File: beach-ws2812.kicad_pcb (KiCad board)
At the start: 4 copper layers, 260 x 120 mm, 103 parts, among them CON101 BARREL_JACK, P101 CONN_01X03, SW101 Pushbutton, SW102 Pushbutton, U101 STM32F103C(8-B)Tx, U102 LM1117-3.3, U103 MAX811, X101 8MHz

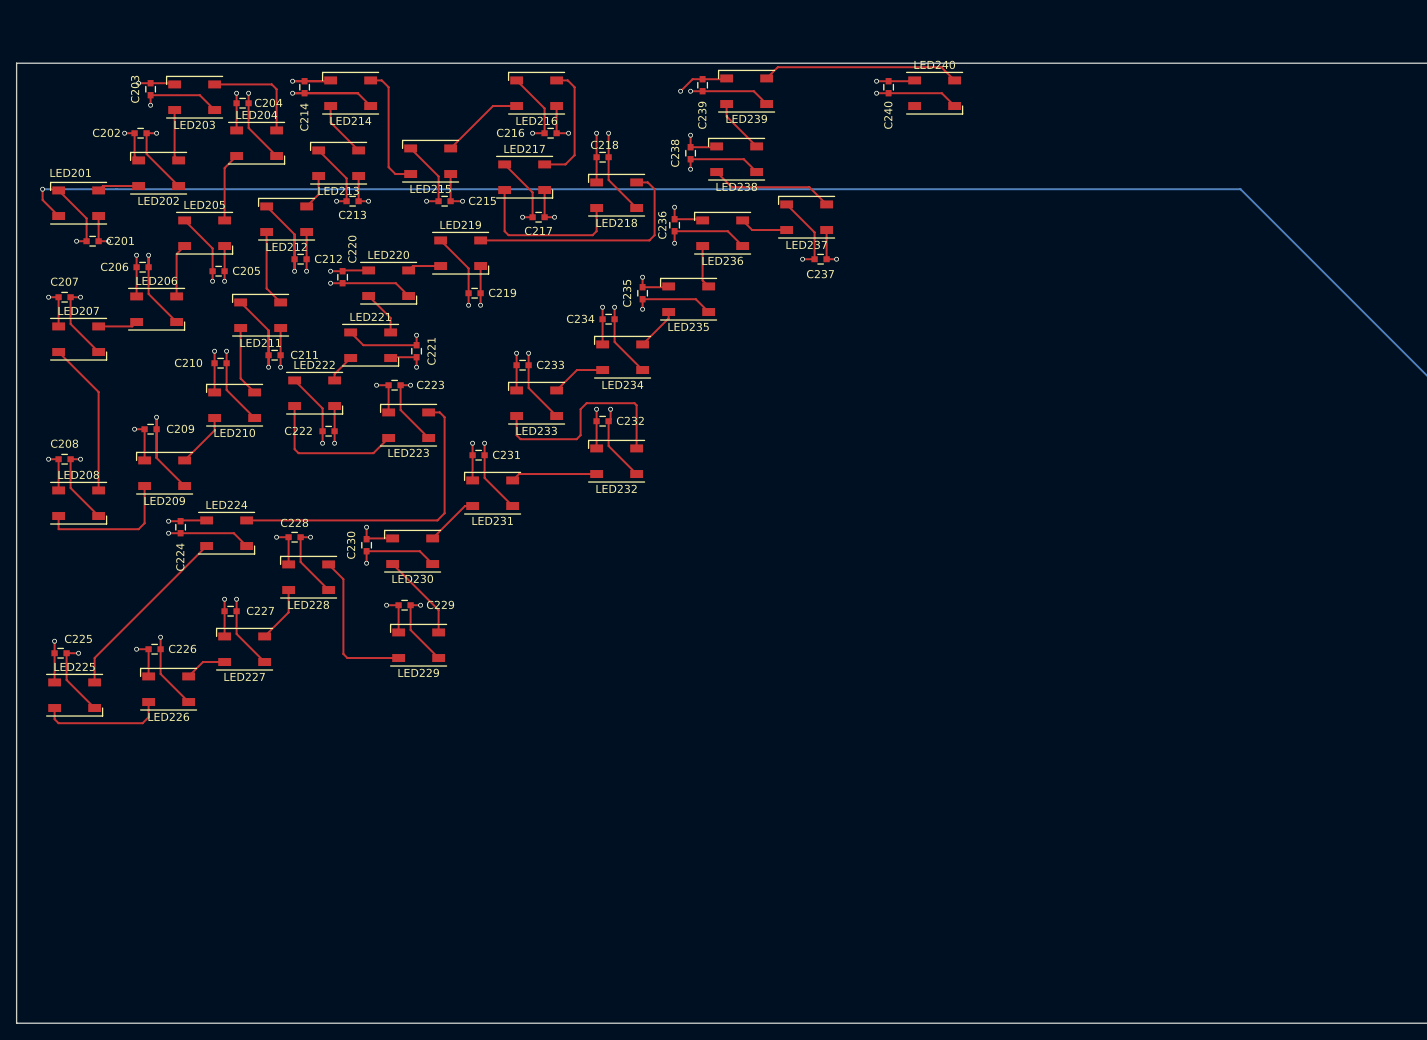
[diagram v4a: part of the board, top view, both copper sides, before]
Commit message: 80 LEDs placed and routed.
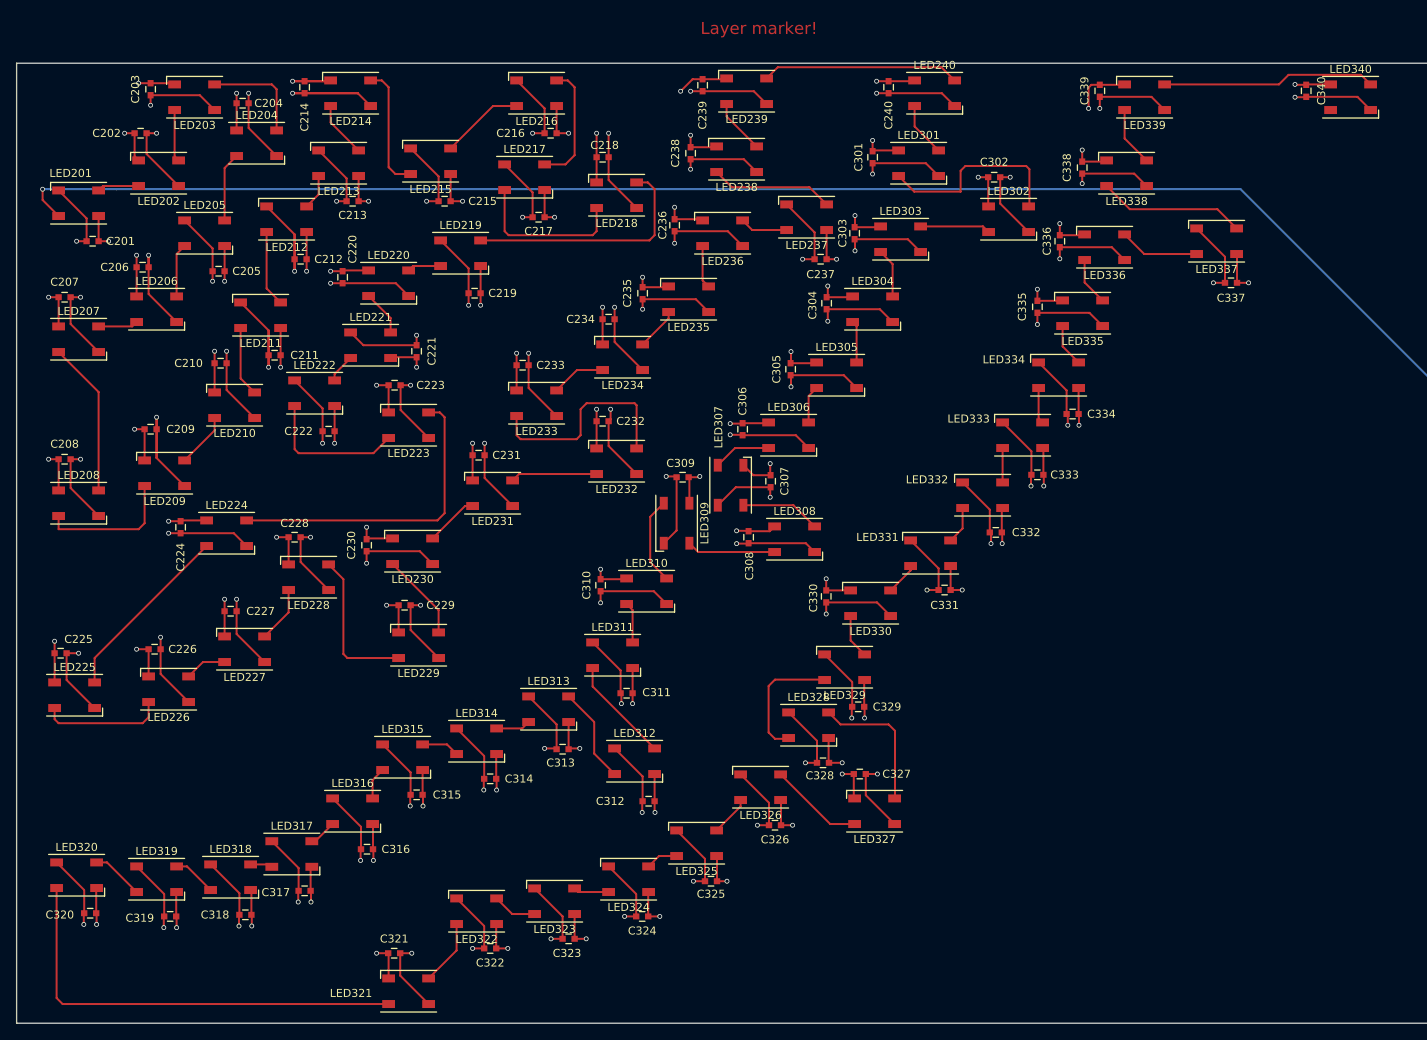
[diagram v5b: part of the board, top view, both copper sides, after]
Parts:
- added C301: 100nF, Capacitors_SMD:C_0603, F.Cu at (127.0, 30.5)
- added C302: 100nF, Capacitors_SMD:C_0603, F.Cu at (142.2, 33.0)
- added C303: 100nF, Capacitors_SMD:C_0603, F.Cu at (124.8, 40.0)
- added C304: 100nF, Capacitors_SMD:C_0603, F.Cu at (121.2, 48.8)
- added C305: 100nF, Capacitors_SMD:C_0603, F.Cu at (116.8, 57.0)
- added C306: 100nF, Capacitors_SMD:C_0603, F.Cu at (110.8, 64.5)
- added C307: 100nF, Capacitors_SMD:C_0603, F.Cu at (114.2, 71.0)
- added C308: 100nF, Capacitors_SMD:C_0603, F.Cu at (111.5, 78.0)
- added C309: 100nF, Capacitors_SMD:C_0603, F.Cu at (103.2, 70.5)
- added C310: 100nF, Capacitors_SMD:C_0603, F.Cu at (93.0, 84.0)
- added C311: 100nF, Capacitors_SMD:C_0603, F.Cu at (96.2, 97.5)
- added C312: 100nF, Capacitors_SMD:C_0603, F.Cu at (99.0, 111.0)
- added C313: 100nF, Capacitors_SMD:C_0603, F.Cu at (88.2, 104.5)
- added C314: 100nF, Capacitors_SMD:C_0603, F.Cu at (79.2, 108.2)
- added C315: 100nF, Capacitors_SMD:C_0603, F.Cu at (70.0, 110.2)
- added C316: 100nF, Capacitors_SMD:C_0603, F.Cu at (63.8, 117.0)
- added C317: 100nF, Capacitors_SMD:C_0603, F.Cu at (56.0, 122.2)
- added C318: 100nF, Capacitors_SMD:C_0603, F.Cu at (48.6, 125.2)
- added C319: 100nF, Capacitors_SMD:C_0603, F.Cu at (39.2, 125.4)
- added C320: 100nF, Capacitors_SMD:C_0603, F.Cu at (29.2, 125.0)
- added C321: 100nF, Capacitors_SMD:C_0603, F.Cu at (67.2, 130.0)
- added C322: 100nF, Capacitors_SMD:C_0603, F.Cu at (79.2, 129.4)
- added C323: 100nF, Capacitors_SMD:C_0603, F.Cu at (89.0, 128.2)
- added C324: 100nF, Capacitors_SMD:C_0603, F.Cu at (98.2, 125.4)
- added C325: 100nF, Capacitors_SMD:C_0603, F.Cu at (106.8, 121.0)
- added C326: 100nF, Capacitors_SMD:C_0603, F.Cu at (114.8, 114.0)
- added C327: 100nF, Capacitors_SMD:C_0603, F.Cu at (125.4, 107.6)
- added C328: 100nF, Capacitors_SMD:C_0603, F.Cu at (120.8, 106.2)
- added C329: 100nF, Capacitors_SMD:C_0603, F.Cu at (125.2, 99.2)
- added C330: 100nF, Capacitors_SMD:C_0603, F.Cu at (121.2, 85.4)
- added C331: 100nF, Capacitors_SMD:C_0603, F.Cu at (136.0, 84.6)
- added C332: 100nF, Capacitors_SMD:C_0603, F.Cu at (142.4, 77.4)
- added C333: 100nF, Capacitors_SMD:C_0603, F.Cu at (147.6, 70.2)
- added C334: 100nF, Capacitors_SMD:C_0603, F.Cu at (152.0, 62.6)
- added C335: 100nF, Capacitors_SMD:C_0603, F.Cu at (147.6, 49.2)
- added C336: 100nF, Capacitors_SMD:C_0603, F.Cu at (150.4, 41.0)
- added C337: 100nF, Capacitors_SMD:C_0603, F.Cu at (171.8, 46.2)
- added C338: 100nF, Capacitors_SMD:C_0603, F.Cu at (153.2, 31.8)
- added C339: 100nF, Capacitors_SMD:C_0603, F.Cu at (155.4, 22.2)
- added C340: 100nF, Capacitors_SMD:C_0603, F.Cu at (181.2, 22.2)
- added LED301: WS2812B, LEDs:LED_WS2812B-PLCC4, F.Cu at (132.8, 31.2)
- added LED302: WS2812B, LEDs:LED_WS2812B-PLCC4, F.Cu at (144.0, 38.2)
- added LED303: WS2812B, LEDs:LED_WS2812B-PLCC4, F.Cu at (130.5, 40.8)
- added LED304: WS2812B, LEDs:LED_WS2812B-PLCC4, F.Cu at (127.0, 49.5)
- added LED305: WS2812B, LEDs:LED_WS2812B-PLCC4, F.Cu at (122.5, 57.8)
- added LED306: WS2812B, LEDs:LED_WS2812B-PLCC4, F.Cu at (116.5, 65.2)
- added LED307: WS2812B, LEDs:LED_WS2812B-PLCC4, F.Cu at (109.2, 71.5)
- added LED308: WS2812B, LEDs:LED_WS2812B-PLCC4, F.Cu at (117.2, 78.2)
- added LED309: WS2812B, LEDs:LED_WS2812B-PLCC4, F.Cu at (102.5, 76.2)
- added LED310: WS2812B, LEDs:LED_WS2812B-PLCC4, F.Cu at (98.8, 84.8)
- added LED311: WS2812B, LEDs:LED_WS2812B-PLCC4, F.Cu at (94.5, 92.8)
- added LED312: WS2812B, LEDs:LED_WS2812B-PLCC4, F.Cu at (97.2, 106.0)
- added LED313: WS2812B, LEDs:LED_WS2812B-PLCC4, F.Cu at (86.5, 99.5)
- added LED314: WS2812B, LEDs:LED_WS2812B-PLCC4, F.Cu at (77.5, 103.5)
- added LED315: WS2812B, LEDs:LED_WS2812B-PLCC4, F.Cu at (68.2, 105.5)
- added LED316: WS2812B, LEDs:LED_WS2812B-PLCC4, F.Cu at (62.0, 112.2)
- added LED317: WS2812B, LEDs:LED_WS2812B-PLCC4, F.Cu at (54.4, 117.6)
- added LED318: WS2812B, LEDs:LED_WS2812B-PLCC4, F.Cu at (46.8, 120.5)
- added LED319: WS2812B, LEDs:LED_WS2812B-PLCC4, F.Cu at (37.5, 120.8)
- added LED320: WS2812B, LEDs:LED_WS2812B-PLCC4, F.Cu at (27.5, 120.2)
- added LED321: WS2812B, LEDs:LED_WS2812B-PLCC4, F.Cu at (69.0, 134.8)
- added LED322: WS2812B, LEDs:LED_WS2812B-PLCC4, F.Cu at (77.5, 124.8)
- added LED323: WS2812B, LEDs:LED_WS2812B-PLCC4, F.Cu at (87.2, 123.5)
- added LED324: WS2812B, LEDs:LED_WS2812B-PLCC4, F.Cu at (96.5, 120.8)
- added LED325: WS2812B, LEDs:LED_WS2812B-PLCC4, F.Cu at (105.0, 116.2)
- added LED326: WS2812B, LEDs:LED_WS2812B-PLCC4, F.Cu at (113.0, 109.2)
- added LED327: WS2812B, LEDs:LED_WS2812B-PLCC4, F.Cu at (127.2, 112.2)
- added LED328: WS2812B, LEDs:LED_WS2812B-PLCC4, F.Cu at (119.0, 101.5)
- added LED329: WS2812B, LEDs:LED_WS2812B-PLCC4, F.Cu at (123.5, 94.2)
- added LED330: WS2812B, LEDs:LED_WS2812B-PLCC4, F.Cu at (126.8, 86.2)
- added LED331: WS2812B, LEDs:LED_WS2812B-PLCC4, F.Cu at (134.2, 80.0)
- added LED332: WS2812B, LEDs:LED_WS2812B-PLCC4, F.Cu at (140.8, 72.8)
- added LED333: WS2812B, LEDs:LED_WS2812B-PLCC4, F.Cu at (145.8, 65.2)
- added LED334: WS2812B, LEDs:LED_WS2812B-PLCC4, F.Cu at (150.2, 57.8)
- added LED335: WS2812B, LEDs:LED_WS2812B-PLCC4, F.Cu at (153.2, 50.0)
- added LED336: WS2812B, LEDs:LED_WS2812B-PLCC4, F.Cu at (156.0, 41.8)
- added LED337: WS2812B, LEDs:LED_WS2812B-PLCC4, F.Cu at (170.0, 41.0)
- added LED338: WS2812B, LEDs:LED_WS2812B-PLCC4, F.Cu at (158.8, 32.5)
- added LED339: WS2812B, LEDs:LED_WS2812B-PLCC4, F.Cu at (161.0, 23.0)
- added LED340: WS2812B, LEDs:LED_WS2812B-PLCC4, F.Cu at (186.8, 23.0)
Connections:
- LED240 pad 2: Net-(LED240-Pad2) -> LEDDATA2
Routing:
- net GND: track 425.8 -> 731.1 mm, vias 51 -> 91
- net +5V: track 384.3 -> 671.5 mm, vias 41 -> 81
- net Net-(LED320-Pad2): track 0.00 -> 55.6 mm
- net Net-(LED339-Pad2): track 0.00 -> 26.7 mm
- net Net-(LED301-Pad2): track 0.00 -> 24.9 mm
- net Net-(LED337-Pad2): track 0.00 -> 18.4 mm
- net Net-(LED327-Pad2): track 0.00 -> 17.7 mm
- net Net-(LED328-Pad2): track 0.00 -> 16.0 mm
- net Net-(LED311-Pad2): track 0.00 -> 13.3 mm
- net Net-(LED312-Pad2): track 0.00 -> 12.1 mm
- net Net-(LED326-Pad2): track 0.00 -> 11.8 mm
- net Net-(LED308-Pad2): track 0.00 -> 11.1 mm
- net Net-(LED309-Pad2): track 0.00 -> 11.0 mm
- net Net-(LED336-Pad2): track 0.00 -> 10.0 mm
- net Net-(LED307-Pad2): track 0.00 -> 10.00 mm
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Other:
- board text added: "Layer marker!"
